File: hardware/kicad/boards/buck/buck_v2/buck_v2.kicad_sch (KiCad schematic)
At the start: 23 parts, among them J1 MCP PWM, J2 9V Battery, J3 Conn_01x02_Socket, Q1 Q_NMOS, SW1 Switch, U1 LF50_TO220, U2 Optocoupler, U3 LM555xM

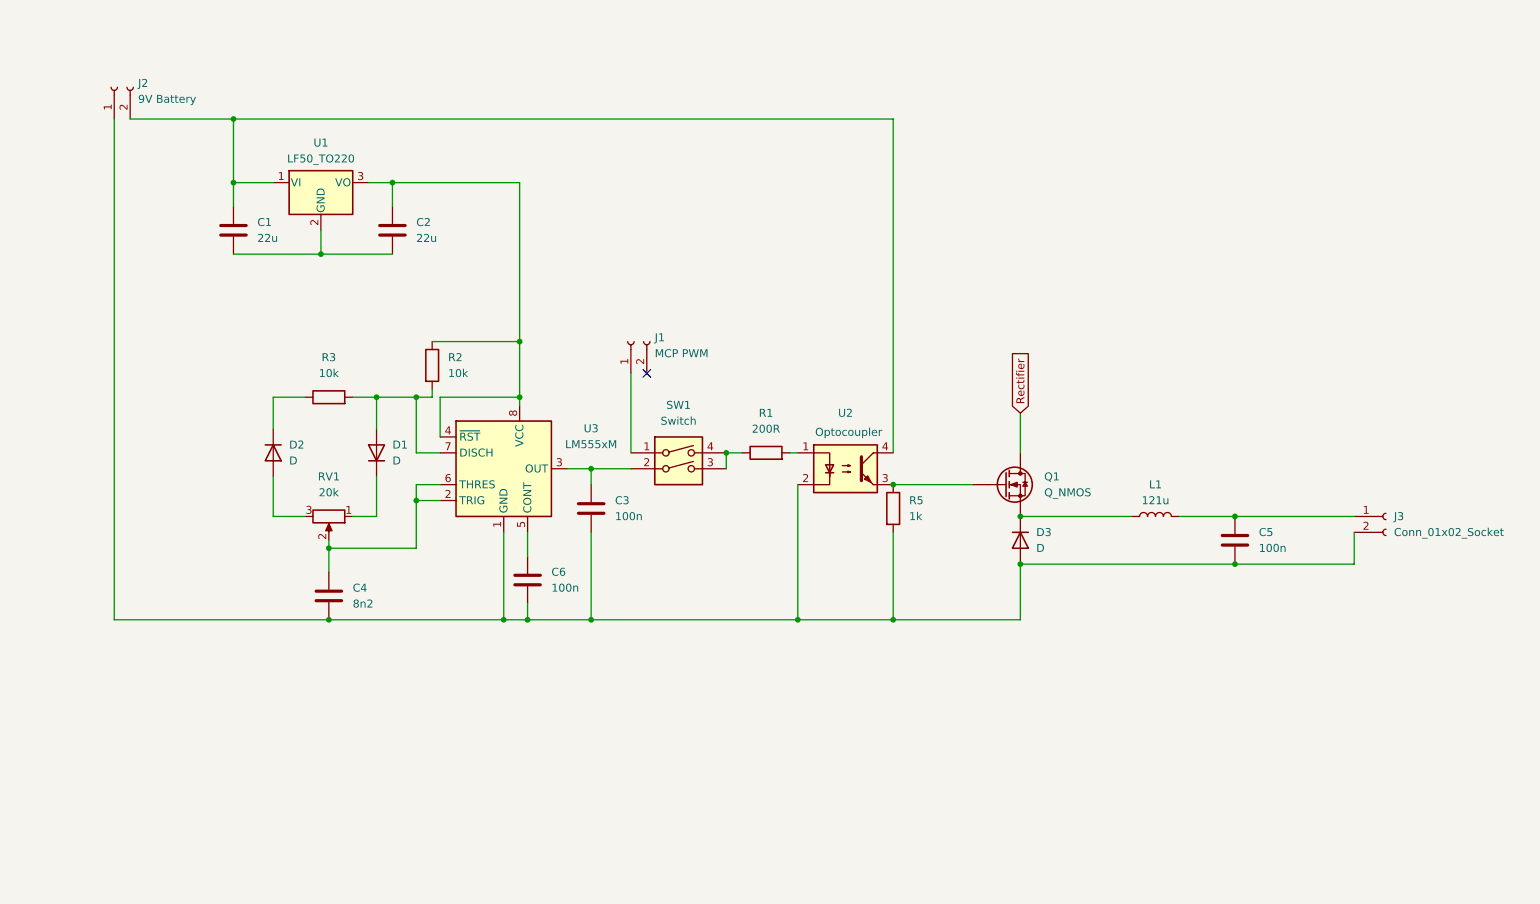
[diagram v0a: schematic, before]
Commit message: Fix buck_v2 gate drive, regulator ground and output cap
Four wiring bugs from review of the new schematic:
- LF50 GND/C1/C2 formed a floating island - regulator had no return, the
  5V rail was undefined. Tied to GND.
- High-side gate drive could not work: opto collector sat on the GND-
  referenced 9V rail and R5 pulled the gate to GND, so V_GS goes negative
  the moment Q1 turns on (drain bus is 15V). The 9V battery now FLOATS on
  the SW node (J2- = SW, J2+ = opto collector, R5 gate->source) like the
  J4 arrangement on buck v1. The LF50/555 control side is fed from the
  Rectifier (V1) rail instead, with C1 as its input cap.
- C5 output cap 100n -> 47u (100n gives volts of ripple at these
  frequencies).
- J1 (MCP PWM) pin 2 was dangling - tied to GND so the PWM input has a
  return path.
ERC: 0 errors (PWR_FLAGs added on Rectifier and GND), only the benign
LM555 lib-mismatch warning left. Note on the sheet explains the floating
gate-drive domain.
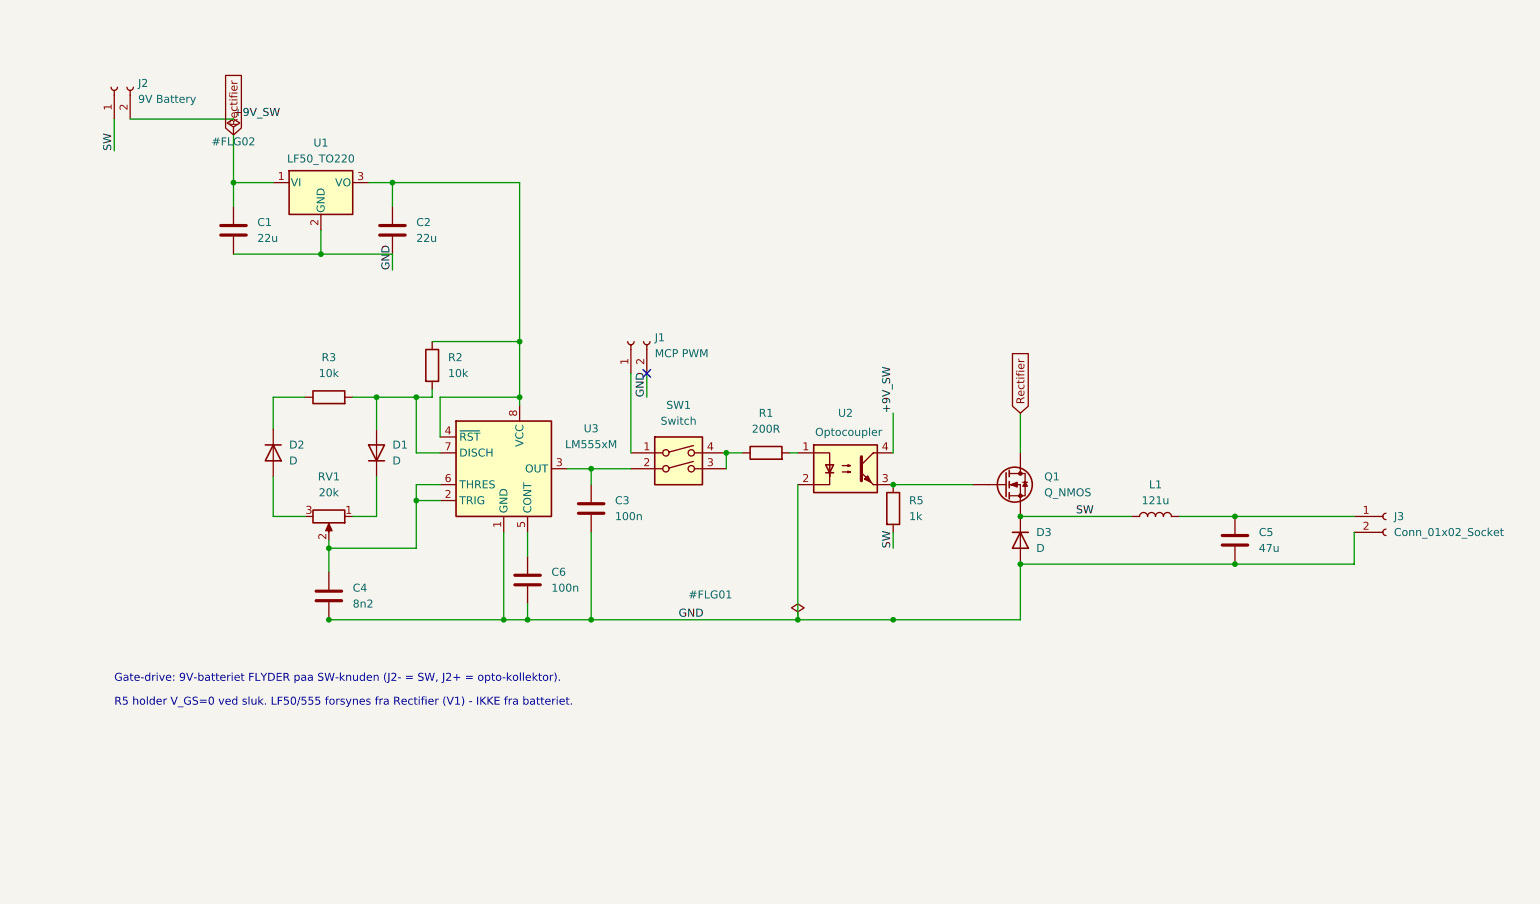
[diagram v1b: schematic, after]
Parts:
- C5: value 100n -> 47u
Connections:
- net Rectifier: now also C1.1, U1.1 (VI)
- net GND: now reaches C1.2, C2.2, U1.2 (GND)
- net GND: now also C3.2, C4.2, C5.2, C6.2, D3.2 (A), J1.2 (Pin_2), J3.2 (Pin_2), U2.2, U3.1 (GND)
- net SW: now reaches D3.1 (K), L1.1, Q1.S
- net SW: now also J2.1 (Pin_1), R5.2
- net +9V_SW: now reaches J2.2 (Pin_2), U2.4
- net +9V_SW: no longer C1.1, U1.1 (VI)
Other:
- note added: "Gate-drive: 9V-batteriet FLYDER paa SW-knuden (J2- = SW, J2+ = opto-kollektor)."
- note added: "R5 holder V_GS=0 ved sluk. LF50/555 forsynes fra Rectifier (V1) - IKKE fra batteriet."

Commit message: Assign THT footprints and shop parts to buck_v2
All footprints set per the fiber-laser rules: LongPads DIPs, LaserPads
TO-220s, the measured 470uH-toroid footprint for L1, screw terminals for
power and pin header for the PWM input. Part values pinned to what the
shop carries: NE555 (DIP-8), 4N25 (DIP-6), LM7805 instead of LF50 (not in
the shop, same pinout), 1N4148 steering diodes, 1N5817 freewheel, IRF530,
20K trimmer (3296W footprint assumed - measure the physical part).

The generic optocoupler symbol had pins numbered 1-4; renumbered to the
4N25 DIP-6 pinout (E=4, C=5) so the netlist lands on the right pads -
pads 3 (NC) and 6 (base) unused. fp-lib-table added for the energy_system
lib. ERC still 0 errors. BOM updated with a buck_v2 section.
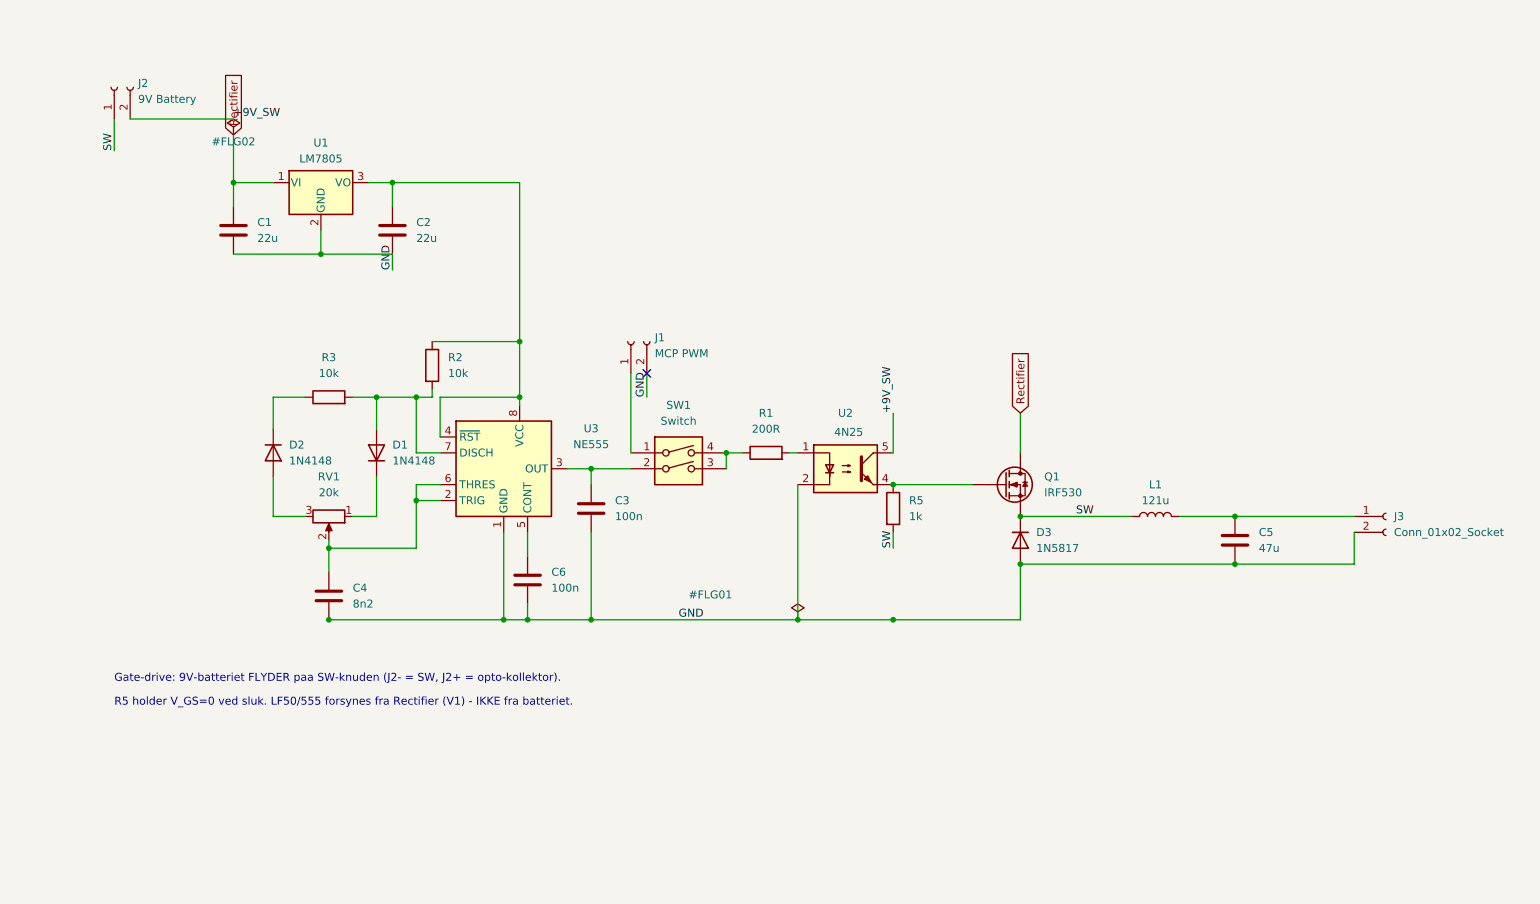
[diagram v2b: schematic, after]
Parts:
- C1, C2, C5: footprint (none) -> Capacitor_THT:CP_Radial_D8.0mm_P3.50mm
- C3, C4, C6: footprint (none) -> Capacitor_THT:C_Disc_D5.0mm_W2.5mm_P5.00mm
- D1, D2: value D -> 1N4148; footprint (none) -> Diode_THT:D_DO-35_SOD27_P7.62mm_Horizontal
- D3: value D -> 1N5817; footprint (none) -> Diode_THT:D_DO-41_SOD81_P10.16mm_Horizontal
- J1: footprint Connector_Wire:SolderWire-0.1sqmm_1x02_P3.6mm_D0.4mm_OD1mm -> Connector_PinHeader_2.54mm:PinHeader_1x02_P2.54mm_Vertical
- J2, J3: footprint Connector_Wire:SolderWire-0.1sqmm_1x02_P3.6mm_D0.4mm_OD1mm -> TerminalBlock:TerminalBlock_bornier-2_P5.08mm
- L1: footprint (none) -> energy_system:L_Toroid_Vertical_L34.5mm_W15.0mm_P28.20mm_LaserPads
- Q1: value Q_NMOS -> IRF530; footprint (none) -> energy_system:TO-220-3_Vertical_LaserPads
- R1, R2, R3, R5: footprint (none) -> Resistor_THT:R_Axial_DIN0207_L6.3mm_D2.5mm_P7.62mm_Horizontal
- RV1: footprint (none) -> Potentiometer_THT:Potentiometer_Bourns_3296W_Vertical
- SW1: footprint (none) -> Button_Switch_THT:SW_DIP_SPSTx02_Slide_9.78x7.26mm_W7.62mm_P2.54mm
- U1: value LF50_TO220 -> LM7805; footprint Package_TO_SOT_SMD:TSOT-23-6 -> energy_system:TO-220-3_Vertical_LaserPads
- U2: value Optocoupler -> 4N25; footprint (none) -> Package_DIP:DIP-6_W7.62mm_LongPads
- U3: value LM555xM -> NE555; footprint Package_SO:SOIC-8_3.9x4.9mm_P1.27mm -> Package_DIP:DIP-8_W7.62mm_LongPads
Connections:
- net +9V_SW: now also U2.5; no longer U2.4
- net at Q1.G, R5.1: now also U2.4; no longer U2.3
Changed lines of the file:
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@@
 			)
 		)
-		(property "Footprint" ""
+		(property "Footprint" "Capacitor_THT:CP_Radial_D8.0mm_P3.50mm"
 			(at 77.1652 49.53 0)
 			(effects
@@
 			)
 		)
-		(property "Footprint" ""
+		(property "Footprint" "Capacitor_THT:C_Disc_D5.0mm_W2.5mm_P5.00mm"
 			(at 98.7552 105.41 0)
 			(effects
@@
 			)
 		)
-		(property "Value" "Q_NMOS"
+		(property "Value" "IRF530"
 			(at 180.34 87.6299 0)
 			(effects
@@
 			)
 		)
-		(property "Footprint" ""
+		(property "Footprint" "energy_system:TO-220-3_Vertical_LaserPads"
 			(at 179.07 83.82 0)
 			(effects
@@
 			)
 		)
-		(property "Footprint" "Connector_Wire:SolderWire-0.1sqmm_1x02_P3.6mm_D0.4mm_OD1mm"
+		(property "Footprint" "TerminalBlock:TerminalBlock_bornier-2_P5.08mm"
 			(at 234.95 91.44 0)
 			(effects
@@
 			)
 		)
-		(property "Footprint" ""
+		(property "Footprint" "Capacitor_THT:CP_Radial_D8.0mm_P3.50mm"
 			(at 211.7852 99.06 0)
 			(effects
@@
 			)
 		)
-		(property "Value" "D"
+		(property "Value" "1N4148"
 			(at 76.2 82.5499 90)
 			(effects
@@
 			)
 		)
-		(property "Footprint" ""
+		(property "Footprint" "Diode_THT:D_DO-35_SOD27_P7.62mm_Horizontal"
 			(at 73.66 81.28 0)
 			(effects
@@
 			)
 		)
-		(property "Footprint" ""
+		(property "Footprint" "Resistor_THT:R_Axial_DIN0207_L6.3mm_D2.5mm_P7.62mm_Horizontal"
 			(at 154.432 90.17 90)
 			(effects
@@
 			)
 		)
-		(property "Footprint" "Connector_Wire:SolderWire-0.1sqmm_1x02_P3.6mm_D0.4mm_OD1mm"
+		(property "Footprint" "TerminalBlock:TerminalBlock_bornier-2_P5.08mm"
 			(at 31.75 22.86 0)
 			(effects
@@
 			)
 		)
-		(property "Footprint" ""
+		(property "Footprint" "Resistor_THT:R_Axial_DIN0207_L6.3mm_D2.5mm_P7.62mm_Horizontal"
 			(at 66.04 74.168 90)
 			(effects
@@
 			)
 		)
-		(property "Footprint" ""
+		(property "Footprint" "Capacitor_THT:C_Disc_D5.0mm_W2.5mm_P5.00mm"
 			(at 67.0052 107.95 0)
 			(effects
@@
 			)
 		)
-		(property "Footprint" ""
+		(property "Footprint" "Capacitor_THT:CP_Radial_D8.0mm_P3.50mm"
 			(at 51.7652 49.53 0)
 			(effects
@@
 			)
 		)
-		(property "Footprint" ""
+		(property "Footprint" "energy_system:L_Toroid_Vertical_L34.5mm_W15.0mm_P28.20mm_LaserPads"
 			(at 198.12 91.44 0)
 			(effects
@@
 			)
 		)
-		(property "Value" "D"
+		(property "Value" "1N4148"
 			(at 59.69 82.5499 90)
 			(effects
@@
 			)
 		)
-		(property "Footprint" ""
+		(property "Footprint" "Diode_THT:D_DO-35_SOD27_P7.62mm_Horizontal"
 			(at 57.15 81.28 0)
 			(effects
@@
 			)
 		)
-		(property "Value" "Optocoupler"
+		(property "Value" "4N25"
 			(at 149.098 77.978 0)
 			(effects
@@
 			)
 		)
-		(property "Footprint" ""
+		(property "Footprint" "Package_DIP:DIP-6_W7.62mm_LongPads"
 			(at 143.51 88.9 0)
 			(effects
@@
 			)
 		)
-		(pin "3"
-		)
-		(pin "1"
-		)
-		(pin "2"
-		)
 		(pin "4"
+		)
+		(pin "1"
+		)
+		(pin "2"
+		)
+		(pin "5"
 		)
 		(instances
@@
 			)
 		)
-		(property "Footprint" ""
+		(property "Footprint" "Button_Switch_THT:SW_DIP_SPSTx02_Slide_9.78x7.26mm_W7.62mm_P2.54mm"
 			(at 121.92 83.82 0)
 			(effects
@@
 			)
 		)
-		(property "Footprint" "Connector_Wire:SolderWire-0.1sqmm_1x02_P3.6mm_D0.4mm_OD1mm"
+		(property "Footprint" "Connector_PinHeader_2.54mm:PinHeader_1x02_P2.54mm_Vertical"
 			(at 114.3 63.5 0)
 			(effects
@@
 			)
 		)
-		(property "Footprint" ""
+		(property "Footprint" "Potentiometer_THT:Potentiometer_Bourns_3296W_Vertical"
 			(at 66.04 91.44 0)
 			(effects
@@
 			)
 		)
-		(property "Value" "D"
+		(property "Value" "1N5817"
 			(at 179.07 96.5199 90)
 			(effects
@@
 			)
 		)
-		(property "Footprint" ""
+		(property "Footprint" "Diode_THT:D_DO-41_SOD81_P10.16mm_Horizontal"
 			(at 176.53 95.25 0)
 			(effects
@@
 			)
 		)
-		(property "Footprint" ""
+		(property "Footprint" "Resistor_THT:R_Axial_DIN0207_L6.3mm_D2.5mm_P7.62mm_Horizontal"
 			(at 80.772 67.31 90)
 			(effects
@@
 			)
 		)
-		(property "Value" "LF50_TO220"
+		(property "Value" "LM7805"
 			(at 64.77 34.29 0)
 			(effects
@@
 			)
 		)
-		(property "Footprint" "Package_TO_SOT_SMD:TSOT-23-6"
+		(property "Footprint" "energy_system:TO-220-3_Vertical_LaserPads"
 			(at 64.77 32.385 0)
 			(effects
@@
 			)
 		)
-		(property "Value" "LM555xM"
+		(property "Value" "NE555"
 			(at 107.95 79.9398 0)
 			(effects
@@
 			)
 		)
-		(property "Footprint" "Package_SO:SOIC-8_3.9x4.9mm_P1.27mm"
+		(property "Footprint" "Package_DIP:DIP-8_W7.62mm_LongPads"
 			(at 93.98 107.95 0)
 			(effects
@@
 			)
 		)
-		(property "Footprint" ""
+		(property "Footprint" "Capacitor_THT:C_Disc_D5.0mm_W2.5mm_P5.00mm"
 			(at 108.9152 93.98 0)
 			(effects
@@
 			)
 		)
-		(property "Footprint" ""
+		(property "Footprint" "Resistor_THT:R_Axial_DIN0207_L6.3mm_D2.5mm_P7.62mm_Horizontal"
 			(at 135.89 83.058 90)
 			(effects

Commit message: buck_v2: skil batteriet fra Rectifier-nettet igen og genbyg printet
Omtegningen ved batteriet havde kortsluttet batteri+ med Rectifier (V1) -
15V-skinnen ville lade 9V-batteriet baglaens, og gate-forsyningens flyden
paa SW var brudt (se forklaringen i PCB-noterne: batteriet maa kun roere
opto-kollektoren og SW). Broen er fjernet; det nye Rectifier-label ved U1
beholdes som V1-foedning til LM7805. PWR_FLAG flyttet med.

PLACE-layoutet og BOM-raekkerne fulgt op paa re-annoteringen (555=U2,
opto=U3, batteri=J1 osv.). Genroutet: 9 topbaner (31 mm), 0 vias, DRC 0
fejl. Nye DXF/gerbers i production/buck_v2/.
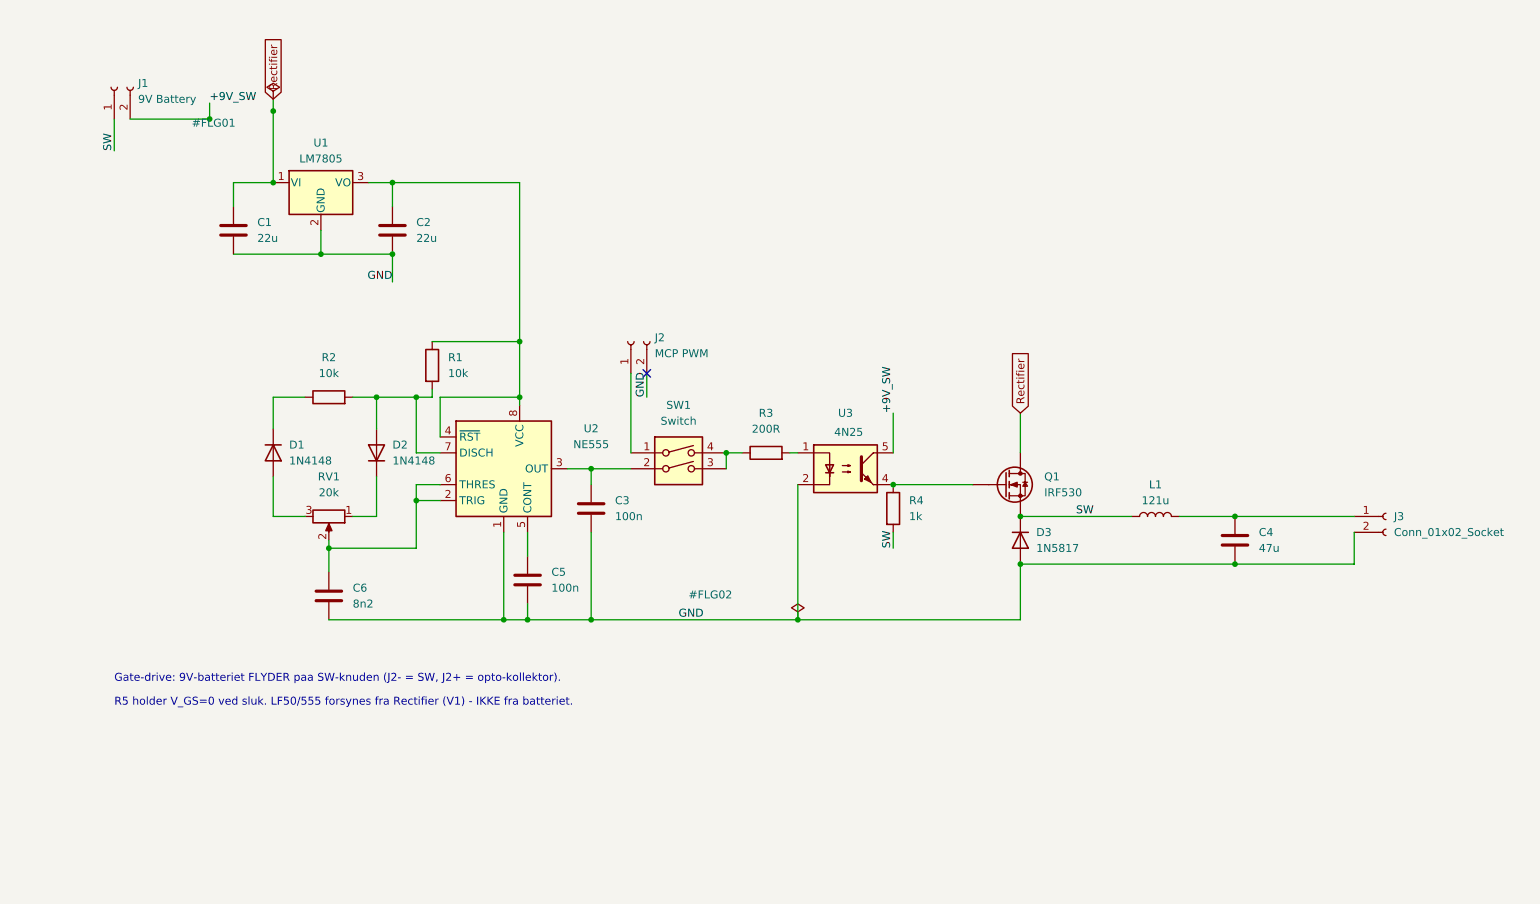
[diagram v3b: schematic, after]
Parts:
- renumbered C5 to C4, C6 to C5, C4 to C6, D2 to D1, D1 to D2, J2 to J1, J1 to J2, R2 to R1, R3 to R2, R1 to R3, R5 to R4, U3 to U2, U2 to U3
